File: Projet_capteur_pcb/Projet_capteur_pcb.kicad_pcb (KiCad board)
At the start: 2 copper layers, 68.6 x 67.9 mm, 21 parts, among them J1 Power, J2 Digital/PWM, J3 Analog, J4 Digital/PWM

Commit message: routageV1 modif
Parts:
- moved R5 1.00 mm to (124.1, 102.0)
- renumbered capteur1 to capteur
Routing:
- net TxD: track 46.4 -> 40.8 mm
- net GND: track 243.3 -> 248.1 mm
- net Rxd: track 43.2 -> 39.4 mm
- net MOSI: track 72.6 -> 70.3 mm
- net SCL: track 9.61 -> 11.6 mm
- net +5V: track 156.9 -> 158.5 mm
- net Net-(AOP1-OUT): track 51.1 -> 52.4 mm
- net potor_out: track 40.1 -> 39.1 mm

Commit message: routageV1
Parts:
- Bluetooth: renamed from Bluetooth1; value ~ -> (none)
- EcranOled1: value ~ -> (none)
- moved capteur 0.50 mm to (132.0, 102.0)
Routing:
- net GND: track 248.1 -> 0.47 mm
- net MOSI: track 70.3 -> 35.3 mm
- net potor_out: track 39.1 -> 59.4 mm, vias 0 -> 1
- net +5V: track 158.5 -> 177.2 mm
- net Net-(AOP1-OUT): track 52.4 -> 46.9 mm
- net Net-(capteur1-OUT): track 4.37 -> 4.87 mm

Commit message: fichier_gerber
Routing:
- net SCK: track 11.4 -> 13.3 mm
- net MOSI: track 35.3 -> 34.1 mm
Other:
- board text added: "MOSI"
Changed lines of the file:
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@@
-			)
-		)
-		(fp_text user "MOSI"
-			(at 1.5 2 270)
-			(unlocked yes)
-			(layer "F.SilkS")
-			(effects
-				(font
-					(size 1 1)
-					(thickness 0.125)
-				)
-				(justify left bottom)
 			)
 		)
@@
 		(layer "Edge.Cuts")
 	)
+	(gr_text "MOSI"
+		(at 134.5 58 270)
+		(layer "F.SilkS")
+		(effects
+			(font
+				(size 1 1)
+				(thickness 0.125)
+			)
+			(justify left bottom)
+		)
+	)
 	(gr_text "GND"
 		(at 159 82.5 0)
@@
 	)
 	(segment
-		(start 134.73 58.73)
-		(end 135 59)
-		(width 0.5)
-		(layer "B.Cu")
-		(net 25)
-	)
-	(segment
-		(start 134.73 56.24)
-		(end 134.73 58.73)
+		(start 134.73 56.73)
+		(end 136.5 58.5)
 		(width 0.5)
 		(layer "B.Cu")
@@
 	)
 	(segment
-		(start 135 59)
+		(start 136.5 58.5)
+		(end 143 58.5)
+		(width 0.5)
+		(layer "B.Cu")
+		(net 25)
+	)
+	(segment
+		(start 134.73 56.24)
+		(end 134.73 56.73)
+		(width 0.5)
+		(layer "B.Cu")
+		(net 25)
+	)
+	(segment
+		(start 143 58.5)
 		(end 143.5 59)
 		(width 0.5)
@@
 	)
 	(segment
-		(start 137.27 55.911844)
-		(end 132.159156 50.801)
+		(start 137.27 52.77)
+		(end 135.301 50.801)
 		(width 0.5)
 		(layer "B.Cu")
@@
 	)
 	(segment
-		(start 132.159156 50.801)
+		(start 135.301 50.801)
 		(end 130.557 50.801)
 		(width 0.5)
@@
 	(segment
 		(start 137.27 56.24)
-		(end 137.27 55.911844)
-		(width 0.5)
-		(layer "B.Cu")
+		(end 137.27 52.77)
+		(width 0.5)
+		(layer "B.Cu")

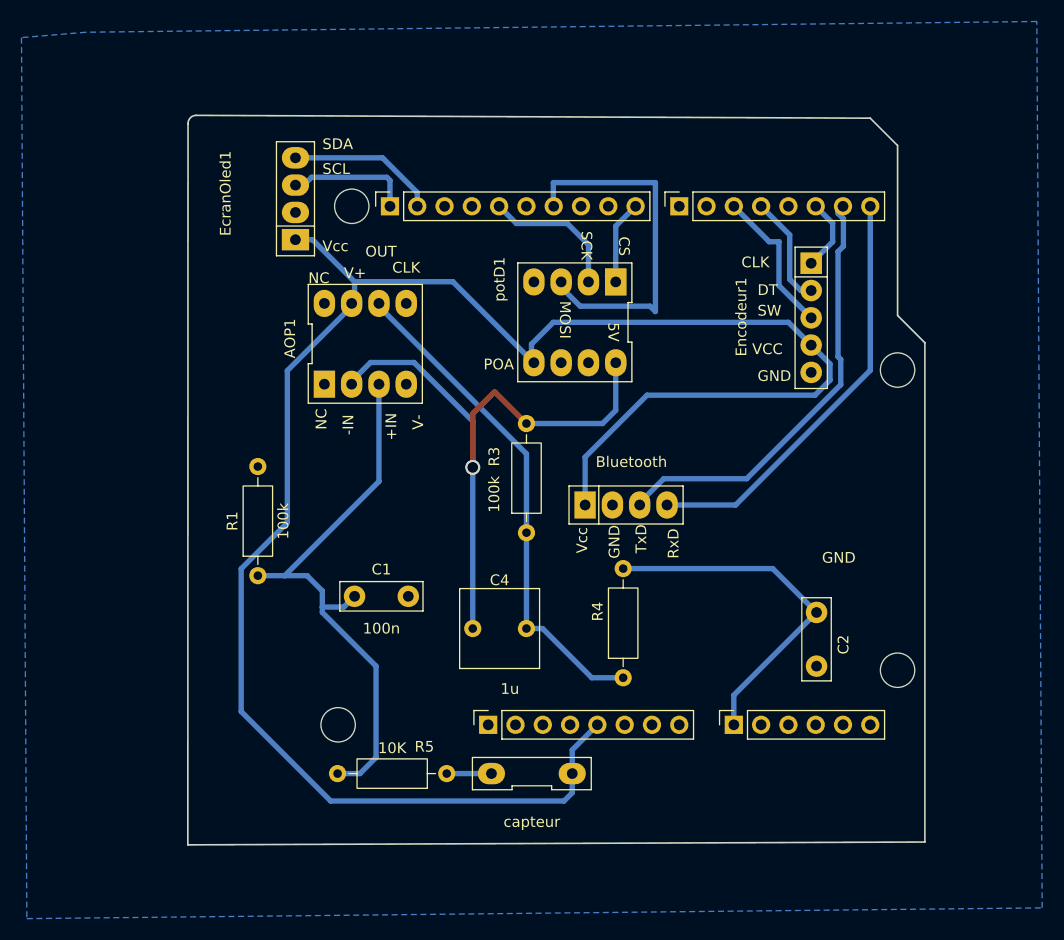
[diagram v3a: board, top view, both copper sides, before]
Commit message: changement-dim-pad
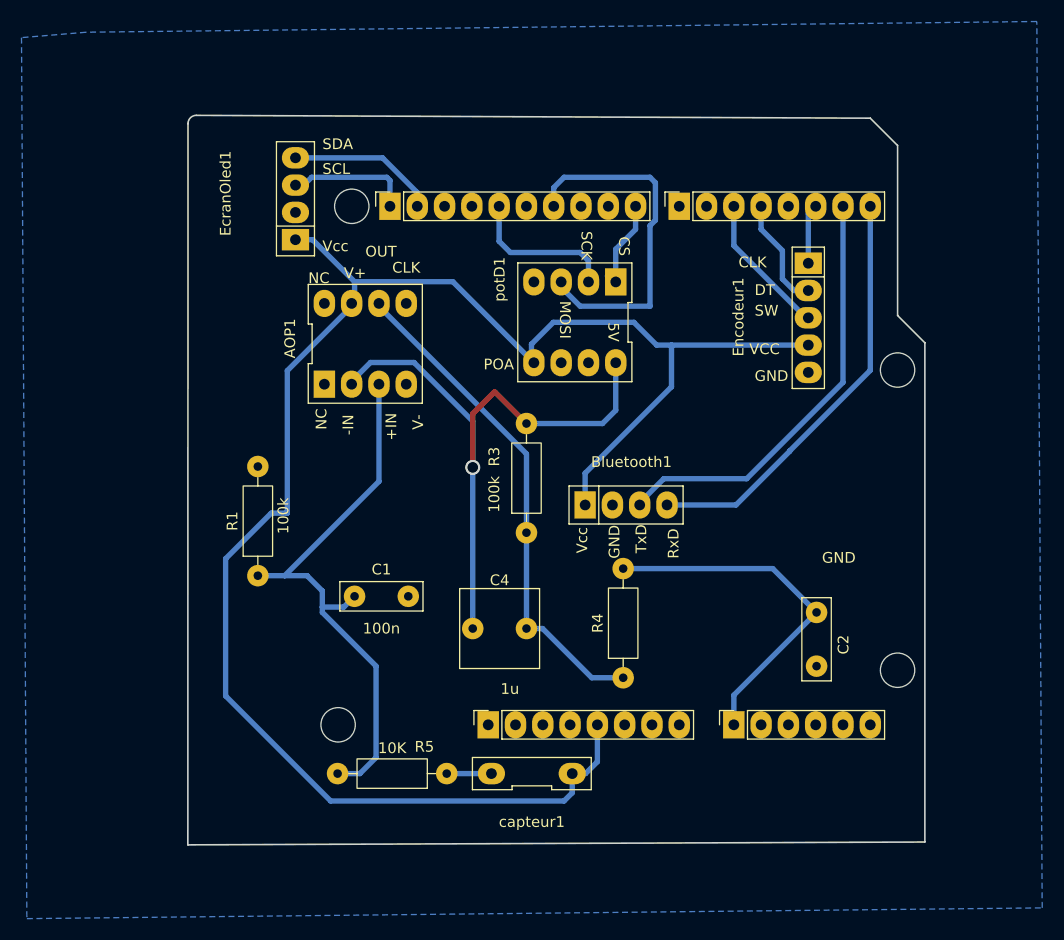
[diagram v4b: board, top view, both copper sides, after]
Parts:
- Bluetooth1: renamed from Bluetooth; value (none) -> ~
- EcranOled1: value (none) -> ~
- moved Encodeur1 0.27 mm to (157.7, 59.6)
- renumbered capteur to capteur1
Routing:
- net +5V: track 177.2 -> 163.7 mm
- net CLK: track 6.78 -> 5.59 mm
- net DT: track 10.3 -> 11.4 mm
- net SCK: track 13.3 -> 14.3 mm
- net MOSI: track 34.1 -> 33.3 mm
- net SW: track 13.9 -> 13.4 mm
